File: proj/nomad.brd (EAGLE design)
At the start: 20.3 x 15.2 mm, 20 parts, among them P7 5.5V-VUSB-GND, P8 5.5V-BOOST_IN-GND, U2 TPS61200S-PVSON-N10, U3 MAX1811SO8

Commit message: Added Solder Jumper to Nomad module to select charge current (open = 500mA / closed = 100mA) @open #13 @close #13
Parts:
- added J1: 100mA, dooba:SMD_JMP
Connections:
- net GND: now also J1.2
- net N$20: now also J1.1
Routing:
- net N$20: track 1.82 -> 6.06 mm, vias 0 -> 2
- net GND: vias 55 -> 54
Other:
- board text removed: "100nF"
- board text removed: "10k"
- board text removed: "10uF"
- board text removed: "1k"
- board text removed: "200k"
- board text removed: "22uF"
- board text removed: "2M"
- board text removed: "4.7uH"
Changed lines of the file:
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@@
 <setting verticaltext="up"/>
 </settings>
-<grid distance="0.005" unitdist="inch" unit="mm" style="lines" multiple="1" display="yes" altdistance="0.025" altunitdist="inch" altunit="inch"/>
+<grid distance="0.005" unitdist="inch" unit="inch" style="lines" multiple="1" display="yes" altdistance="0.025" altunitdist="inch" altunit="inch"/>
 <layers>
 <layer number="1" name="Top" color="4" fill="1" visible="yes" active="yes"/>
@@
 <layer number="115" name="ReferenceISLANDS" color="7" fill="1" visible="yes" active="yes"/>
 <layer number="116" name="Patch_BOT" color="9" fill="4" visible="yes" active="yes"/>
+<layer number="117" name="Refs" color="11" fill="1" visible="yes" active="yes"/>
 <layer number="118" name="Rect_Pads" color="7" fill="1" visible="yes" active="yes"/>
 <layer number="121" name="_tsilk" color="7" fill="1" visible="yes" active="yes"/>
@@
 <wire x1="49.53" y1="59.69" x2="29.21" y2="59.69" width="0" layer="20"/>
 <wire x1="29.21" y1="59.69" x2="29.21" y2="44.45" width="0" layer="20"/>
-<text x="34.036" y="58.42" size="0.8128" layer="21" font="vector" ratio="18" rot="R180">2M</text>
-<text x="49.149" y="54.356" size="0.8128" layer="21" font="vector" ratio="18" rot="R180">10k</text>
 <wire x1="46.355" y1="54.102" x2="46.609" y2="54.102" width="0.254" layer="21"/>
 <wire x1="46.609" y1="54.102" x2="46.609" y2="57.404" width="0.254" layer="21"/>
 <wire x1="46.609" y1="57.404" x2="46.355" y2="57.404" width="0.254" layer="21"/>
 <wire x1="46.609" y1="54.102" x2="46.736" y2="53.975" width="0.254" layer="21"/>
-<text x="40.513" y="49.53" size="0.8128" layer="21" font="vector" ratio="18">10uF</text>
-<text x="42.418" y="52.451" size="0.8128" layer="21" font="vector" ratio="18" rot="R180">1k</text>
-<wire x1="43.434" y1="49.911" x2="44.577" y2="49.911" width="0.254" layer="21"/>
-<wire x1="40.259" y1="49.911" x2="40.132" y2="49.911" width="0.254" layer="21"/>
-<wire x1="40.132" y1="49.911" x2="39.37" y2="50.673" width="0.254" layer="21"/>
-<text x="32.766" y="54.483" size="0.8128" layer="21" font="vector" ratio="18" rot="R90">200k</text>
-<text x="35.56" y="48.133" size="0.8128" layer="21" font="vector" ratio="18">2M</text>
-<text x="34.036" y="45.466" size="0.8128" layer="21" font="vector" ratio="18" rot="R135">200k</text>
-<text x="39.243" y="49.657" size="0.8128" layer="21" font="vector" ratio="18" rot="R270">22uF</text>
-<text x="41.529" y="44.704" size="0.8128" layer="21" font="vector" ratio="18">4.7uH</text>
 <rectangle x1="36.195" y1="56.515" x2="37.465" y2="57.531" layer="21"/>
 <rectangle x1="32.385" y1="48.26" x2="33.655" y2="49.276" layer="21"/>
-<text x="47.244" y="45.847" size="0.8128" layer="22" font="vector" ratio="18" rot="MR0">100nF</text>
-<rectangle x1="42.799" y1="45.847" x2="43.434" y2="46.482" layer="22"/>
 <rectangle x1="45.204378125" y1="45.280578125" x2="46.296578125" y2="45.285659375" layer="21"/>
 <rectangle x1="45.1993" y1="45.285659375" x2="46.30165625" y2="45.290734375" layer="21"/>
@@
 <element name="U2" library="dooba" package="S-PVSON-N10" value="TPS61200S-PVSON-N10" x="35.306" y="52.832"/>
 <element name="U3" library="dooba" package="SO8" value="MAX1811SO8" x="41.148" y="57.15" rot="R90"/>
+<element name="J1" library="dooba" package="SMD_JMP" value="100mA" x="48.006" y="53.34"/>
 </elements>
 <signals>
@@
 <via x="46.99" y="52.07" extent="1-16" drill="0.3302"/>
 <via x="48.895" y="52.197" extent="1-16" drill="0.3302"/>
-<via x="48.006" y="53.34" extent="1-16" drill="0.3302"/>
 <via x="43.815" y="47.625" extent="1-16" drill="0.3302"/>
 <via x="41.529" y="45.212" extent="1-16" drill="0.3302"/>
@@
 <via x="36.068" y="53.213" extent="1-16" drill="0.3302"/>
 <via x="35.306" y="52.451" extent="1-16" drill="0.3302"/>
+<contactref element="J1" pad="2"/>
 </signal>
 <signal name="N$13">
@@
 <wire x1="43.688" y1="56.515" x2="45.355" y2="56.515" width="0.254" layer="1"/>
 <wire x1="45.355" y1="56.515" x2="45.466" y2="56.404" width="0.254" layer="1"/>
+<contactref element="J1" pad="1"/>
+<wire x1="45.466" y1="56.404" x2="45.577" y2="56.404" width="0.254" layer="1"/>
+<wire x1="45.577" y1="56.404" x2="45.593" y2="56.388" width="0.254" layer="1"/>
+<via x="45.593" y="56.388" extent="1-16" drill="0.3556"/>
+<wire x1="45.593" y1="56.388" x2="45.593" y2="54.61" width="0.254" layer="16"/>
+<wire x1="45.593" y1="54.61" x2="46.863" y2="53.34" width="0.254" layer="16"/>
+<via x="46.863" y="53.34" extent="1-16" drill="0.3556"/>
+<wire x1="46.863" y1="53.34" x2="47.387" y2="53.34" width="0.254" layer="1"/>
 </signal>
 <signal name="VBAT">

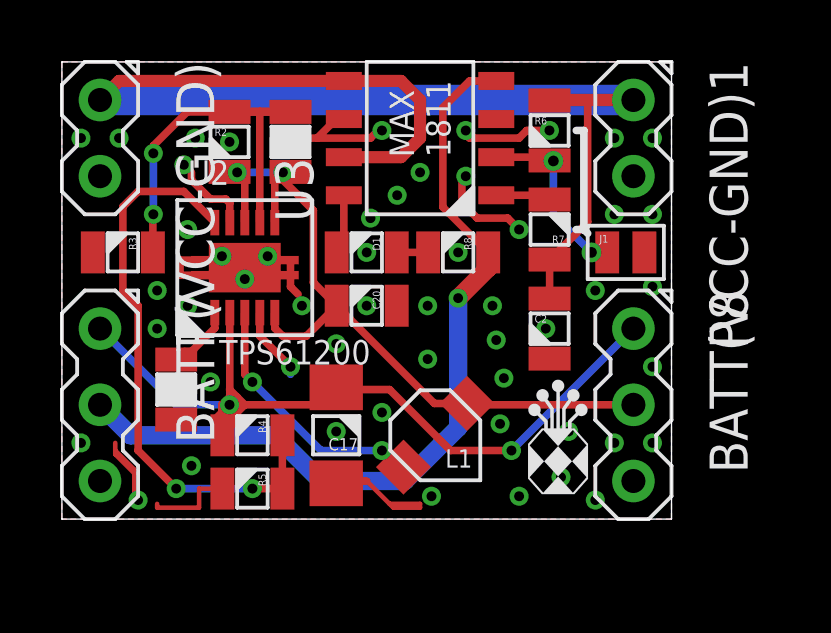
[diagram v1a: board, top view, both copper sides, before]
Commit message: Completed new Shiva board using SPI for MicroSD and Aecho Improved some QFN parts in the Eagle Library Added ref layer to Nomad for ZFPCBA @close #7
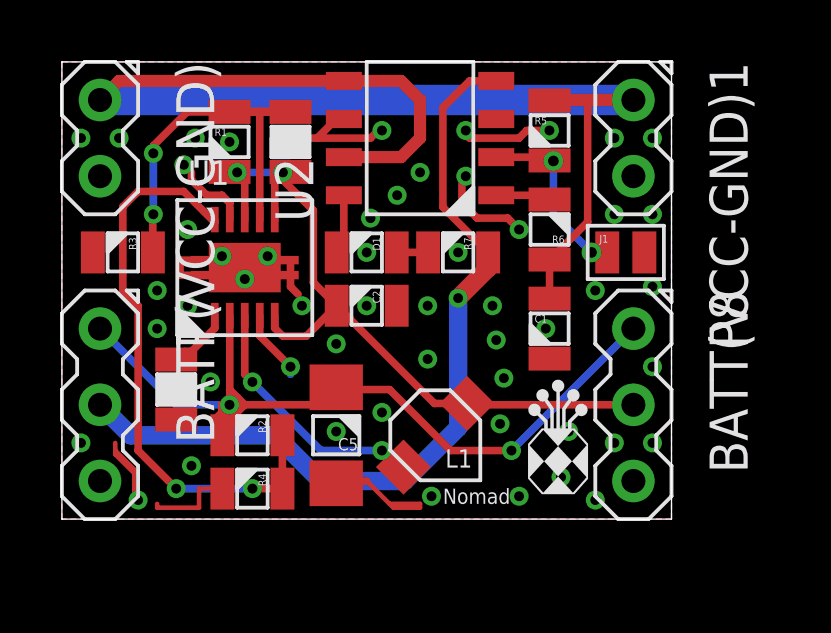
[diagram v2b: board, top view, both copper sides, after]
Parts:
- removed C20: 10uF, dooba:0805
- removed R8: 1k, dooba:0805
- removed U3: MAX1811SO8, dooba:SO8
- added C1: 10uF, dooba:0805
- added R1: 2M, dooba:0805
- added U1: TPS61200S-PVSON-N10, dooba:S-PVSON-N10
- R4: value 2M -> 200k
- R5: value 200k -> 10k
- R7: value 10k -> 1k
- U2: value TPS61200S-PVSON-N10 -> MAX1811SO8; device dooba:S-PVSON-N10 -> dooba:SO8
- moved R5 15.5 mm to (45.5, 57.4), turned to 270 degrees
- moved R2 9.81 mm to (35.6, 47.2), turned to 180 degrees
- moved U2 7.26 mm to (41.1, 57.1), turned to 90 degrees
- moved C2 6.14 mm to (39.4, 51.6), turned to 180 degrees
- moved R6 3.30 mm to (45.5, 54.1), turned to 90 degrees
- moved R7 3.14 mm to (42.4, 53.3), turned to 180 degrees
- moved R4 1.78 mm to (35.6, 45.5)
- renumbered C17 to C5, C18 to C3, C19 to C4
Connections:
- net 5.5V: now also R2.2, U1.2; no longer R4.2, U2.2
- net BOOST_IN: now also C2.2, R1.2, U1.5, U1.6, U1.8; no longer C20.2, R2.2, U2.5, U2.6, U2.8
- net GND: now also C1.2, C2.1, R4.2, U1.4, U1.9, U1.PAD, U1.PAD0, U1.PAD1, U1.PAD2, U1.PAD3, U2.P$3, U2.P$6; no longer C2.2, C20.1, R5.2, U2.4, U2.9, U2.PAD, U2.PAD0, U2.PAD1, U2.PAD2, U2.PAD3, U3.P$3, U3.P$6
- net N$13: now also R1.1, U1.7; no longer R2.1, U2.7
- net N$14: now also R2.1, U1.10; no longer R5.1, U2.10
- net N$15: now also U1.1; no longer U2.1
- net N$16: now also U1.3; no longer U2.3
- net N$17: now also U2.P$8; no longer U3.P$8
- net N$18: now also R7.2; no longer R8.2
- net N$19: now also R6.2, U2.P$1; no longer R7.2, U3.P$1
- net N$20: now also R5.2, U2.P$2; no longer R6.2, U3.P$2
- net VBAT: now also C1.1, R5.1, U2.P$5, U2.P$7; no longer C2.1, R7.1, U3.P$5, U3.P$7
- net VUSB: now also R7.1, U2.P$4; no longer R8.1, U3.P$4
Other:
- board text added: "C1"
- board text added: "C2"
- board text added: "C3"
- board text added: "C4"
- board text added: "C5"
- board text added: "D1"
- board text added: "L1"
- board text added: "Nomad"
- board text added: "R1"
- board text added: "R2"
- board text added: "R3"
- board text added: "R4"
- board text added: "R5"
- board text added: "R6"
- board text added: "R7"
- board text added: "U1"
- board text added: "U2"
- board text removed: "MAX 1811"
- board text removed: "TPS61200"
